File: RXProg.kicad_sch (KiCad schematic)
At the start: 7 parts, among them J1 DIP-28, J2 Pin, J3 Pin, U1 STM32G474CETx, U2 SN74ALVC164245DL, U3 LSF0108BQ, U4 MIC5317-3.3xM5

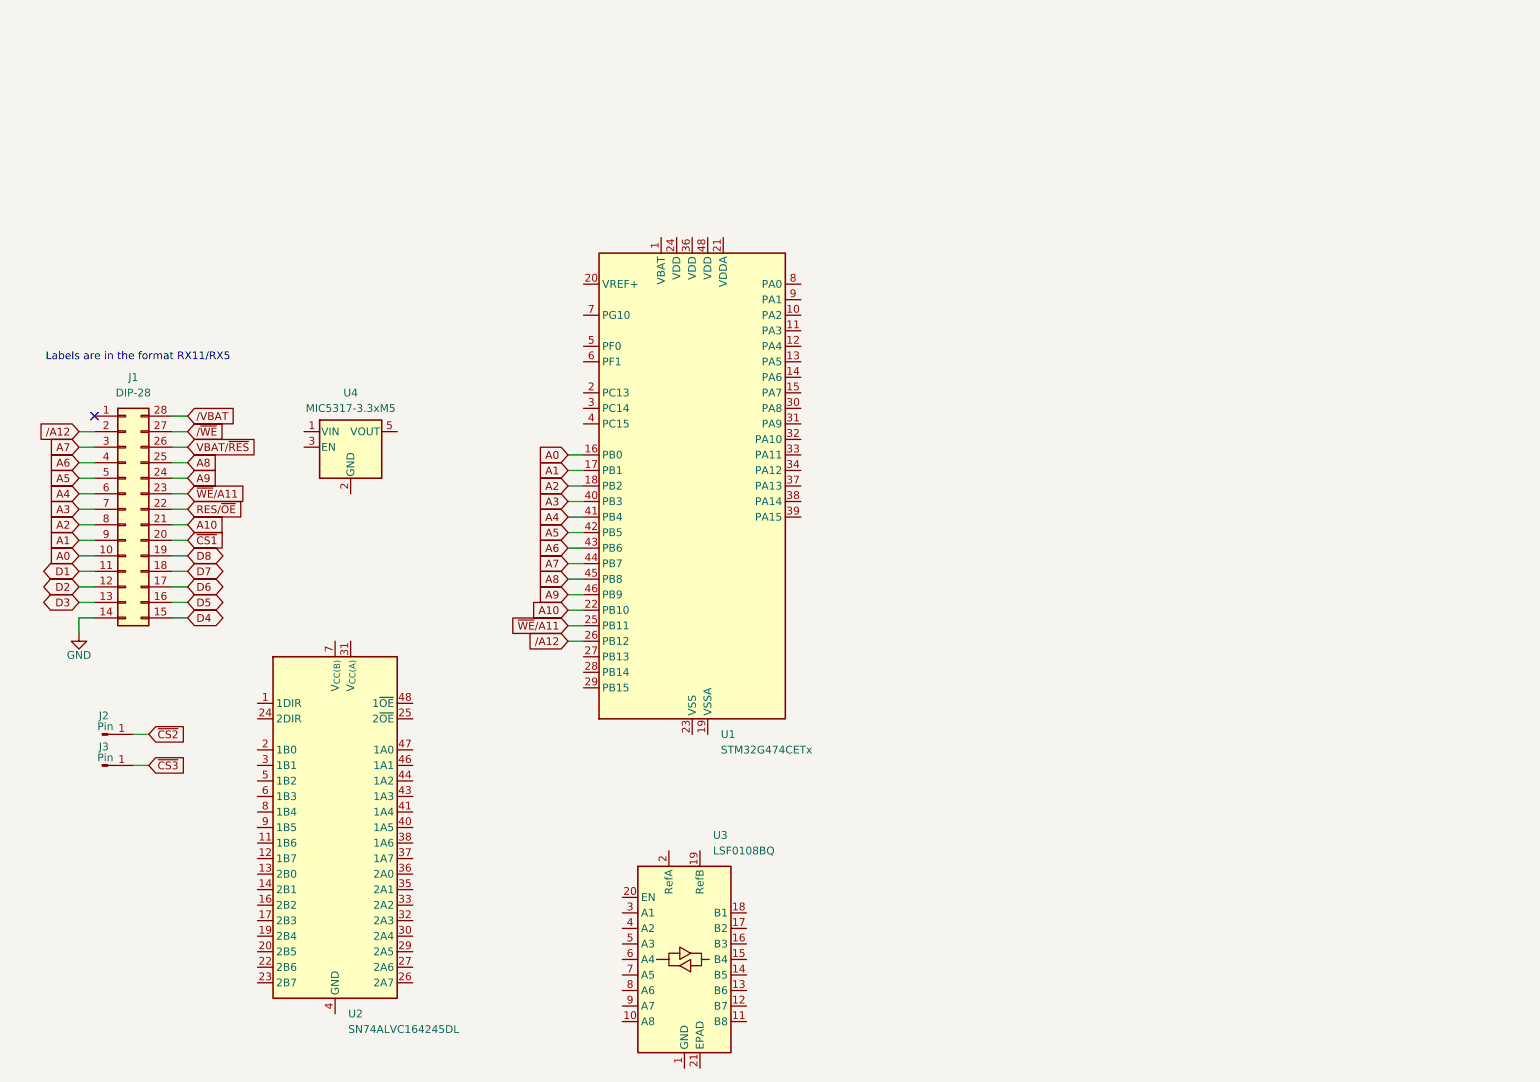
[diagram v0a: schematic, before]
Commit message: Add level shifters
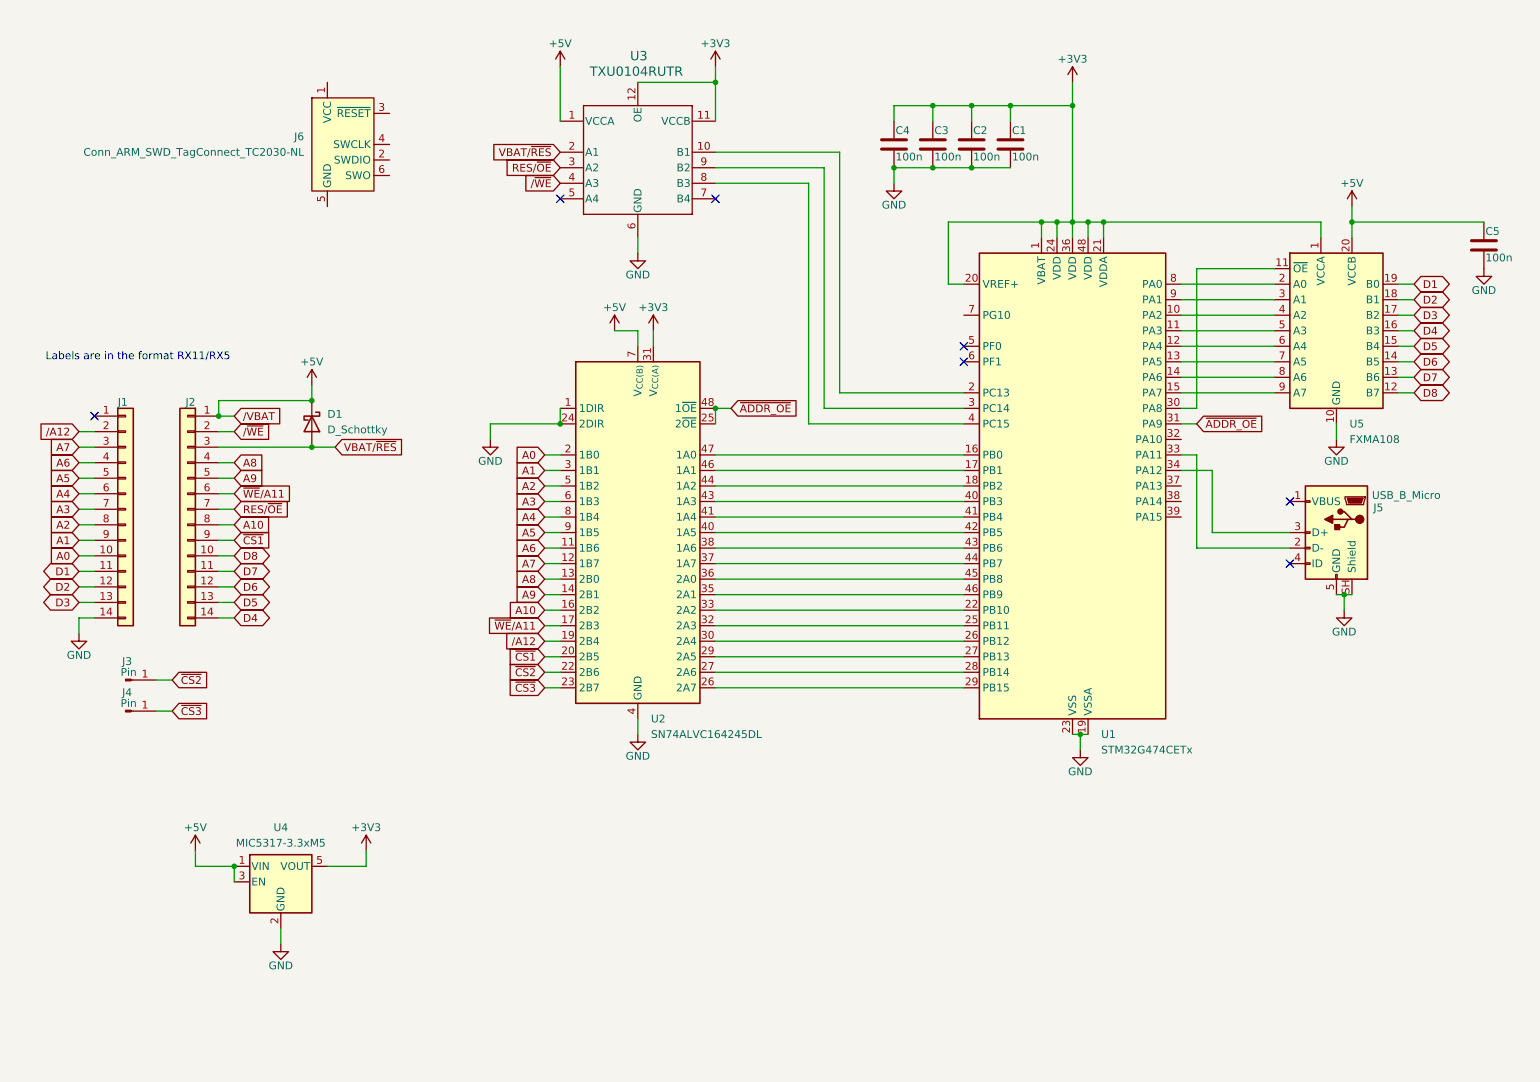
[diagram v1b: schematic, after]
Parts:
- removed J1: DIP-28, Package_DIP:DIP-28_W15.24mm, symbol Connector_Generic:Conn_02x14_Counter_Clockwise
- removed U3: LSF0108BQ, Package_DFN_QFN:DHVQFN-20-1EP_2.5x4.5mm_P0.5mm_EP1x3mm, symbol Logic_LevelTranslator:LSF0108BQ
- added C1, C2, C3, C4, C5: 100n, Capacitor_SMD:C_0402_1005Metric, symbol Device:C
- added D1: D_Schottky, symbol Device:D_Schottky
- added J1, J2: Conn_01x14, Connector_PinHeader_2.54mm:PinHeader_1x14_P2.54mm_Vertical, symbol Connector_Generic:Conn_01x14
- added J5: USB_B_Micro, Connector_USB:USB_Micro-B_Amphenol_10103594-0001LF_Horizontal, symbol Connector:USB_B_Micro
- added J6: Conn_ARM_SWD_TagConnect_TC2030-NL, Connector:Tag-Connect_TC2030-IDC-NL_2x03_P1.27mm_Vertical, symbol Connector:Conn_ARM_SWD_TagConnect_TC2030-NL
- added U3: TXU0104RUTR, footprints:QFN_04RUTR_TEX, symbol TXU0104RUTR:TXU0104RUTR
- added U5: FXMA108, Package_DFN_QFN:WQFN-20-1EP_2.5x4.5mm_P0.5mm_EP1x2.9mm, symbol Logic_LevelTranslator:FXMA108
- J3: renamed from J2; footprint (none) -> Connector_Pin:Pin_D0.9mm_L10.0mm_W2.4mm_FlatFork
- J4: renamed from J3; footprint (none) -> Connector_Pin:Pin_D0.9mm_L10.0mm_W2.4mm_FlatFork
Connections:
- net A0: now also U2.2 (1B0), J1.10 (Pin_10); no longer U1.16 (PB0)
- net A1: now also U2.3 (1B1), J1.9 (Pin_9); no longer U1.17 (PB1)
- net A10: now also U2.16 (2B2), J2.8 (Pin_8); no longer U1.22 (PB10)
- net A2: now also U2.5 (1B2), J1.8 (Pin_8); no longer U1.18 (PB2)
- net A3: now also U2.6 (1B3), J1.7 (Pin_7); no longer U1.40 (PB3)
- net A4: now also U2.8 (1B4), J1.6 (Pin_6); no longer U1.41 (PB4)
- net A5: now also U2.9 (1B5), J1.5 (Pin_5); no longer U1.42 (PB5)
- net A6: now also U2.11 (1B6), J1.4 (Pin_4); no longer U1.43 (PB6)
- net A7: now also U2.12 (1B7), J1.3 (Pin_3); no longer U1.44 (PB7)
- net A8: now also U2.13 (2B0), J2.4 (Pin_4); no longer U1.45 (PB8)
- net A9: now also U2.14 (2B1), J2.5 (Pin_5); no longer U1.46 (PB9)
- net D1: now also J1.11 (Pin_11), U5.19 (B0)
- net D2: now also J1.12 (Pin_12), U5.18 (B1)
- net D3: now also J1.13 (Pin_13), U5.17 (B2)
- net D4: now also J2.14 (Pin_14), U5.16 (B3)
- net D5: now also J2.13 (Pin_13), U5.15 (B4)
- net D6: now also J2.12 (Pin_12), U5.14 (B5)
- net D7: now also J2.11 (Pin_11), U5.13 (B6)
- net D8: now also J2.10 (Pin_10), U5.12 (B7)
- net GND: now also U1.19 (VSSA), U1.23 (VSS), U1.35 (VSS), U1.47 (VSS), U2.1 (1DIR), U2.10 (GND), U2.15 (GND), U2.21 (GND), U2.24 (2DIR), U2.28 (GND), U2.34 (GND), U2.39 (GND), U2.4 (GND), U2.45 (GND), U4.2 (GND), C1.2, C2.2, C3.2, C4.2, C5.2, J1.14 (Pin_14), J5.5 (GND), J5.SH (Shield), U3.6 (GND), U5.10 (GND)
- net RES/~{OE}: now also J2.7 (Pin_7), U3.3 (A2)
- net VBAT/~{RES}: now also D1.2 (A), J2.3 (Pin_3), U3.2 (A1)
- net /A12: now also U2.19 (2B4), J1.2 (Pin_2); no longer U1.26 (PB12)
- net /~{WE}: now also J2.2 (Pin_2), U3.4 (A3)
- net ~{CS1}: now also U2.20 (2B5), J2.9 (Pin_9)
- net ~{CS2}: now also U2.22 (2B6)
- net ~{CS3}: now also U2.23 (2B7)
- net ~{WE}/A11: now also U2.17 (2B3), J2.6 (Pin_6); no longer U1.25 (PB11)
- net +5V: now reaches U2.18 (V_{CC(B)}), U2.7 (V_{CC(B)})
- net +5V: now also U4.1 (VIN), U4.3 (EN), C5.1, D1.1 (K), J2.1 (Pin_1), U3.1 (VCCA), U5.20 (VCCB)
- net ~{ADDR_OE}: now reaches U2.25 (2~{OE})
- net ~{ADDR_OE}: now also U1.31 (PA9), U2.48 (1~{OE})
- net at U2.26 (2A7): now also U1.29 (PB15)
- net at U2.27 (2A6): now also U1.28 (PB14)
- net at U2.29 (2A5): now also U1.27 (PB13)
- net at U2.30 (2A4): now also U1.26 (PB12)
- net +3V3: now reaches U2.31 (V_{CC(A)}), U2.42 (V_{CC(A)})
- net +3V3: now also U1.1 (VBAT), U1.20 (VREF+), U1.21 (VDDA), U1.24 (VDD), U1.36 (VDD), U1.48 (VDD), U4.5 (VOUT), C1.1, C2.1, C3.1, C4.1, U3.11 (VCCB), U3.12 (OE), U5.1 (VCCA)
- net at U2.32 (2A3): now also U1.25 (PB11)
- net at U2.33 (2A2): now also U1.22 (PB10)
- net at U2.35 (2A1): now also U1.46 (PB9)
- net at U2.36 (2A0): now also U1.45 (PB8)
- net at U2.37 (1A7): now also U1.44 (PB7)
- net at U2.38 (1A6): now also U1.43 (PB6)
- net at U2.40 (1A5): now also U1.42 (PB5)
- net at U2.41 (1A4): now also U1.41 (PB4)
- net at U2.43 (1A3): now also U1.40 (PB3)
- net at U2.44 (1A2): now also U1.18 (PB2)
- net at U2.46 (1A1): now also U1.17 (PB1)
- net at U2.47 (1A0): now also U1.16 (PB0)
- net at U1.10 (PA2): now also U5.4 (A2)
- net at U1.11 (PA3): now also U5.5 (A3)
- net at U1.12 (PA4): now also U5.6 (A4)
- net at U1.13 (PA5): now also U5.7 (A5)
- net at U1.14 (PA6): now also U5.8 (A6)
- net at U1.15 (PA7): now also U5.9 (A7)
- net at U1.2 (PC13): now also U3.10 (B1)
- net at U1.3 (PC14): now also U3.9 (B2)
- net at U1.30 (PA8): now also U5.11 (~{OE})
- net at U1.33 (PA11): now also J5.2 (D-)
- net at U1.34 (PA12): now also J5.3 (D+)
- net at U1.4 (PC15): now also U3.8 (B3)
- net at U1.8 (PA0): now also U5.2 (A0)
- net at U1.9 (PA1): now also U5.3 (A1)
- no-connect marks 1 -> 7
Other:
- moved on the sheet: J3, J4, U1, U2, U4

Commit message: Add
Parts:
- added C7, C8: 10u, Capacitor_SMD:C_0402_1005Metric, symbol Device:C
- D1: value D_Schottky -> CD214A-B140LR; footprint (none) -> footprints:CD214A
- J6: value Conn_ARM_SWD_TagConnect_TC2030-NL -> SWD
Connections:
- net +3V3: now also J6.1 (VCC), C8.1
- net +5V: now also C7.1
- net GND: now also J6.5 (GND), C7.2, C8.2
- net ~{FRAM_CS}: now reaches U1.32 (PA10)
- net at U1.37 (PA13): now also J6.2 (SWDIO)
- net at U1.38 (PA14): now also J6.4 (SWCLK)
- net ~{NRST}: now reaches U1.7 (PG10)
- net ~{NRST}: now also J6.3 (~{RESET})
- no-connect marks 7 -> 8
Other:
- moved on the sheet: J5, J6

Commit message: Start routing
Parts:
- added C10, C11, C6, C9: 100n, Capacitor_SMD:C_0201_0603Metric, symbol Device:C
- added JP1: RX5_Select, Jumper:SolderJumper-2_P1.3mm_Open_RoundedPad1.0x1.5mm, symbol Jumper:SolderJumper_2_Open
- C1, C2, C3, C4, C5: footprint Capacitor_SMD:C_0402_1005Metric -> Capacitor_SMD:C_0201_0603Metric
- C7, C8: value 10u -> 1u; footprint Capacitor_SMD:C_0402_1005Metric -> Capacitor_SMD:C_0201_0603Metric
- D1: value CD214A-B140LR -> RB531SM-30T2R; footprint footprints:CD214A -> Diode_SMD:D_SOD-523
- J3, J4: footprint Connector_Pin:Pin_D0.9mm_L10.0mm_W2.4mm_FlatFork -> footprints:Pin
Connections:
- net +3V3: now also C11.1, C9.1
- net +5V: now also C10.1, C6.1
- net GND: now also C10.2, C11.2, C6.2, C9.2, JP1.1 (A)
- net D_-: now reaches J5.2 (D-), U1.33 (PA11)
- net D_+: now reaches J5.3 (D+), U1.34 (PA12)
- net at U1.39 (PA15): now also JP1.2 (B)

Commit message: Finished routing
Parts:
- added C12: 100n, Capacitor_SMD:C_0201_0603Metric, symbol Device:C
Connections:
- net +3V3: now also C12.1
- net GND: now also C12.2
- net ~{FRAM_CS}: no longer names the net of U1.32 (PA10)
- no-connect marks 8 -> 9
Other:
- moved on the sheet: C5

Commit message: Finish routing (again)
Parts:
- removed U2: SN74ALVC164245DL, Package_SO:SSOP-48_7.5x15.9mm_P0.635mm, symbol 74xx:SN74ALVC164245DL
- added U2: SN74ALVC164245DGG, Package_SO:TSSOP-48_6.1x12.5mm_P0.5mm, symbol 74xx:SN74ALVC164245DGG
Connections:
- net +3V3: now also U2.31 (V_{CC(A)}), U2.42 (V_{CC(A)})
- net +5V: now also U2.18 (V_{CC(B)}), U2.7 (V_{CC(B)})
- net A0: now also U2.2 (1B0)
- net A1: now also U2.3 (1B1)
- net A10: now also U2.16 (2B2)
- net A2: now also U2.5 (1B2)
- net A3: now also U2.6 (1B3)
- net A4: now also U2.8 (1B4)
- net A5: now also U2.9 (1B5)
- net A6: now also U2.11 (1B6)
- net A7: now also U2.12 (1B7)
- net A8: now also U2.13 (2B0)
- net A9: now also U2.14 (2B1)
- net GND: now also U2.1 (1DIR), U2.10 (GND), U2.15 (GND), U2.21 (GND), U2.24 (2DIR), U2.28 (GND), U2.34 (GND), U2.39 (GND), U2.4 (GND), U2.45 (GND)
- net /A12: now also U2.19 (2B4)
- net ~{ADDR_OE}: now also U2.25 (2~{OE}), U2.48 (1~{OE})
- net ~{CS1}: now also U2.20 (2B5)
- net ~{CS2}: now also U2.22 (2B6)
- net ~{CS3}: now also U2.23 (2B7)
- net ~{WE}/A11: now also U2.17 (2B3)
- net at U1.29 (PB15): now also U2.26 (2A7)
- net at U1.28 (PB14): now also U2.27 (2A6)
- net at U1.27 (PB13): now also U2.29 (2A5)
- net at U1.26 (PB12): now also U2.30 (2A4)
- net at U1.25 (PB11): now also U2.32 (2A3)
- net at U1.22 (PB10): now also U2.33 (2A2)
- net at U1.46 (PB9): now also U2.35 (2A1)
- net at U1.45 (PB8): now also U2.36 (2A0)
- net at U1.44 (PB7): now also U2.37 (1A7)
- net at U1.43 (PB6): now also U2.38 (1A6)
- net at U1.42 (PB5): now also U2.40 (1A5)
- net at U1.41 (PB4): now also U2.41 (1A4)
- net at U1.40 (PB3): now also U2.43 (1A3)
- net at U1.18 (PB2): now also U2.44 (1A2)
- net at U1.17 (PB1): now also U2.46 (1A1)
- net at U1.16 (PB0): now also U2.47 (1A0)
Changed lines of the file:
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@@
 	)
 	(junction
-		(at 195.58 27.94)
+		(at 111.76 80.01)
 		(diameter 0)
 		(color 0 0 0 0)
 	)
 	(junction
-		(at 137.16 77.47)
+		(at 195.58 27.94)
 		(diameter 0)
 		(color 0 0 0 0)
@@
 	)
 	(junction
-		(at 111.76 80.01)
-		(diameter 0)
-		(color 0 0 0 0)
-	)
-	(junction
 		(at 55.88 78.74)
 		(diameter 0)
@@
 	)
 	(junction
+		(at 137.16 77.47)
+		(diameter 0)
+		(color 0 0 0 0)
+	)
+	(junction
 		(at 58.42 152.4)
 		(diameter 0)
@@
 	)
 	(symbol
-		(lib_id "74xx:SN74ALVC164245DL")
-		(at 124.46 97.79 0)
-		(unit 1)
-		(body_style 1)
-		(exclude_from_sim no)
-		(in_bom yes)
-		(on_board yes)
-		(in_pos_files yes)
-		(dnp no)
-		(fields_autoplaced yes)
-		(property "Reference" "U2"
-			(at 126.6033 128.27 0)
-			(show_name no)
-			(do_not_autoplace no)
-			(effects
-				(font
-					(size 1.27 1.27)
-				)
-				(justify left)
-			)
-		)
-		(property "Value" "SN74ALVC164245DL"
-			(at 126.6033 130.81 0)
-			(show_name no)
-			(do_not_autoplace no)
-			(effects
-				(font
-					(size 1.27 1.27)
-				)
-				(justify left)
-			)
-		)
-		(property "Footprint" "Package_SO:SSOP-48_7.5x15.9mm_P0.635mm"
-			(at 124.46 99.06 0)
-			(hide yes)
-			(show_name no)
-			(do_not_autoplace no)
-			(effects
-				(font
-					(size 1.27 1.27)
-					(italic yes)
-				)
-			)
-		)
-		(property "Datasheet" "https://www.ti.com/lit/ds/symlink/sn74alvc164245.pdf"
-			(at 124.46 101.6 0)
-			(hide yes)
-			(show_name no)
-			(do_not_autoplace no)
-			(effects
-				(font
-					(size 1.27 1.27)
-				)
-			)
-		)
-		(property "Description" "16-Bit 2.5V to 3.3V or 3.3V to 5V Level-Shifting Transceiver With 3-State Outputs, SSOP-48"
-			(at 124.46 97.79 0)
-			(hide yes)
-			(show_name no)
-			(do_not_autoplace no)
-			(effects
-				(font
-					(size 1.27 1.27)
-				)
-			)
-		)
-		(pin "32"
-		)
-		(pin "30"
-		)
-		(pin "23"
-		)
-		(pin "26"
-		)
-		(pin "27"
-		)
-		(pin "37"
-		)
-		(pin "42"
-		)
-		(pin "31"
-		)
-		(pin "28"
-		)
-		(pin "29"
-		)
-		(pin "20"
-		)
-		(pin "18"
-		)
-		(pin "22"
-		)
-		(pin "45"
-		)
-		(pin "43"
-		)
-		(pin "48"
-		)
-		(pin "46"
-		)
-		(pin "40"
-		)
-		(pin "17"
-		)
-		(pin "19"
-		)
-		(pin "39"
-		)
-		(pin "21"
-		)
-		(pin "24"
-		)
-		(pin "25"
-		)
-		(pin "36"
-		)
-		(pin "35"
-		)
-		(pin "38"
-		)
-		(pin "41"
-		)
-		(pin "34"
-		)
-		(pin "33"
-		)
-		(pin "44"
-		)
-		(pin "47"
-		)
-		(pin "1"
-		)
-		(pin "2"
-		)
-		(pin "3"
-		)
-		(pin "4"
-		)
-		(pin "5"
-		)
-		(pin "6"
-		)
-		(pin "7"
-		)
-		(pin "8"
-		)
-		(pin "9"
-		)
-		(pin "10"
-		)
-		(pin "11"
-		)
-		(pin "12"
-		)
-		(pin "13"
-		)
-		(pin "14"
-		)
-		(pin "15"
-		)
-		(pin "16"
-		)
-		(instances
-			(project "RXProg"
-				(path "/6941a808-9eb1-402d-8d55-36c0ef9498d8"
-					(reference "U2")
-					(unit 1)
-				)
-			)
-		)
-	)
-	(symbol
 		(lib_id "Connector:USB_B_Micro")
 		(at 251.46 97.79 0)
@@
 					(unit 1)
 				)
+			)
+		)
+	)
+	(symbol
+		(lib_id "74xx:SN74ALVC164245DGG")
+		(at 124.46 97.79 0)
+		(unit 1)
+		(body_style 1)
+		(exclude_from_sim no)
+		(in_bom yes)
+		(on_board yes)
+		(in_pos_files yes)
+		(dnp no)
+		(fields_autoplaced yes)
+		(property "Reference" "U2"
+			(at 126.6033 128.27 0)
+			(show_name no)
+			(do_not_autoplace no)
+			(effects
+				(font
+					(size 1.27 1.27)
+				)
+				(justify left)
+			)
+		)
+		(property "Value" "SN74ALVC164245DGG"
+			(at 126.6033 130.81 0)
+			(show_name no)
+			(do_not_autoplace no)
+			(effects
+				(font
+					(size 1.27 1.27)
+				)
+				(justify left)
+			)
+		)
+		(property "Footprint" "Package_SO:TSSOP-48_6.1x12.5mm_P0.5mm"
+			(at 124.46 99.06 0)
+			(hide yes)
+			(show_name no)
+			(do_not_autoplace no)
+			(effects
+				(font
+					(size 1.27 1.27)
+					(italic yes)
+				)
+			)
+		)
+		(property "Datasheet" "https://www.ti.com/lit/ds/symlink/sn74alvc164245.pdf"
+			(at 124.46 101.6 0)
+			(hide yes)
+			(show_name no)
+			(do_not_autoplace no)
+			(effects
+				(font
+					(size 1.27 1.27)
+				)
+			)
+		)
+		(property "Description" "16-Bit 2.5V to 3.3V or 3.3V to 5V Level-Shifting Transceiver With 3-State Outputs, TSSOP-48"
+			(at 124.46 97.79 0)
+			(hide yes)
+			(show_name no)
+			(do_not_autoplace no)
+			(effects
+				(font
+					(size 1.27 1.27)
+				)
+			)
+		)
+		(pin "37"
+		)
+		(pin "42"
+		)
+		(pin "35"
+		)
+		(pin "30"
+		)
+		(pin "36"
+		)
+		(pin "38"
+		)
+		(pin "39"
+		)
+		(pin "32"
+		)
+		(pin "29"
+		)
+		(pin "31"
+		)
+		(pin "40"
+		)
+		(pin "33"
+		)
+		(pin "41"
+		)
+		(pin "27"
+		)
+		(pin "28"
+		)
+		(pin "17"
+		)
+		(pin "26"
+		)
+		(pin "25"
+		)
+		(pin "24"
+		)
+		(pin "23"
+		)
+		(pin "22"
+		)
+		(pin "21"
+		)
+		(pin "20"
+		)
+		(pin "19"
+		)
+		(pin "34"
+		)
+		(pin "18"
+		)
+		(pin "48"
+		)
+		(pin "47"
+		)
+		(pin "46"
+		)
+		(pin "45"
+		)
+		(pin "44"
+		)
+		(pin "43"
+		)
+		(pin "10"
+		)
+		(pin "11"
+		)
+		(pin "7"
+		)
+		(pin "13"
+		)
+		(pin "9"
+		)
+		(pin "8"
+		)
+		(pin "12"
+		)
+		(pin "15"
+		)
+		(pin "6"
+		)
+		(pin "5"
+		)
+		(pin "4"
+		)
+		(pin "3"
+		)
+		(pin "2"
+		)
+		(pin "1"
+		)
+		(pin "16"
+		)
+		(pin "14"
+		)
+		(instances
+			(project "RXProg"
+				(path "/6941a808-9eb1-402d-8d55-36c0ef9498d8"
+					(reference "U2")
+					(unit 1)
+				)
